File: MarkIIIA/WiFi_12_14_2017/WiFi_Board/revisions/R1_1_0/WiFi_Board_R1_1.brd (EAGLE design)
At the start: 50.8 x 43.2 mm, 29 parts, among them P1 POWER_JACKPTH, P2 USB-B1HSB6, P3 44764-1201

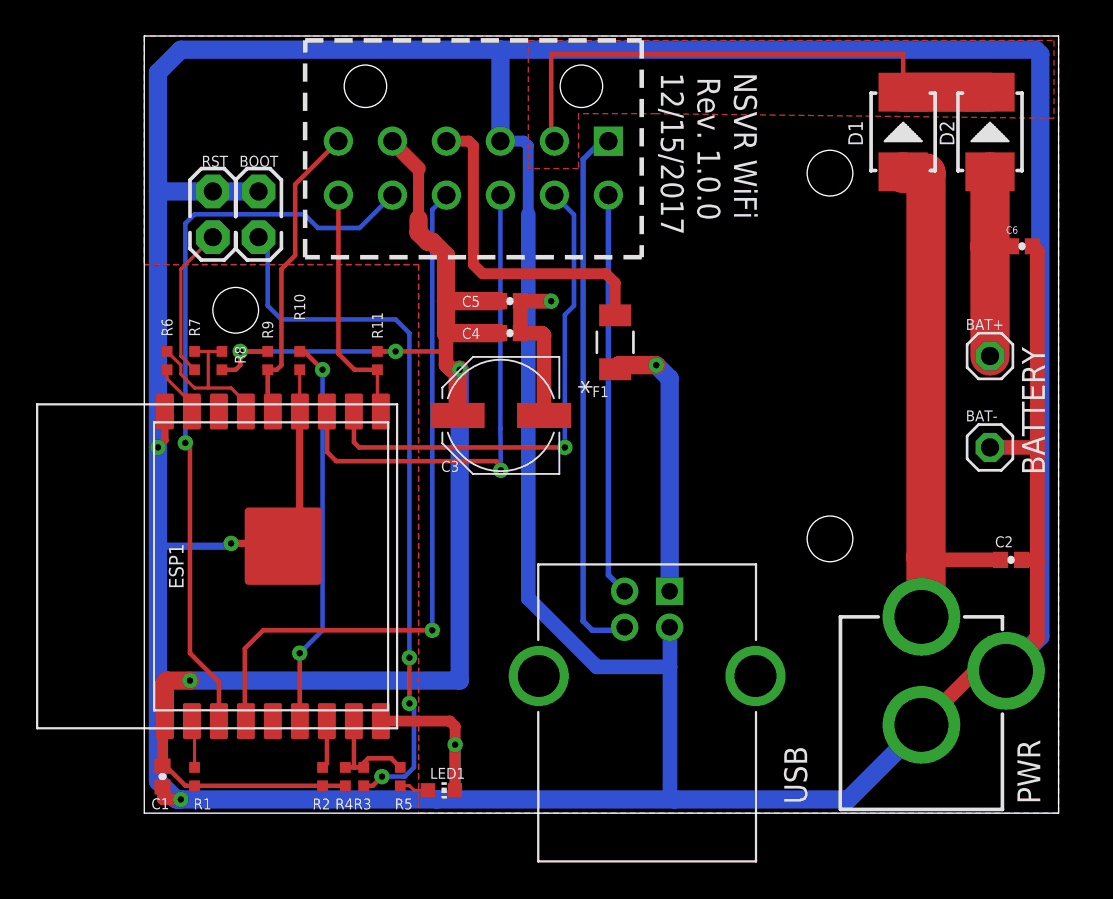
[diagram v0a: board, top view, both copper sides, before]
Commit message: Revise WiFi Board to increase Case Clearance
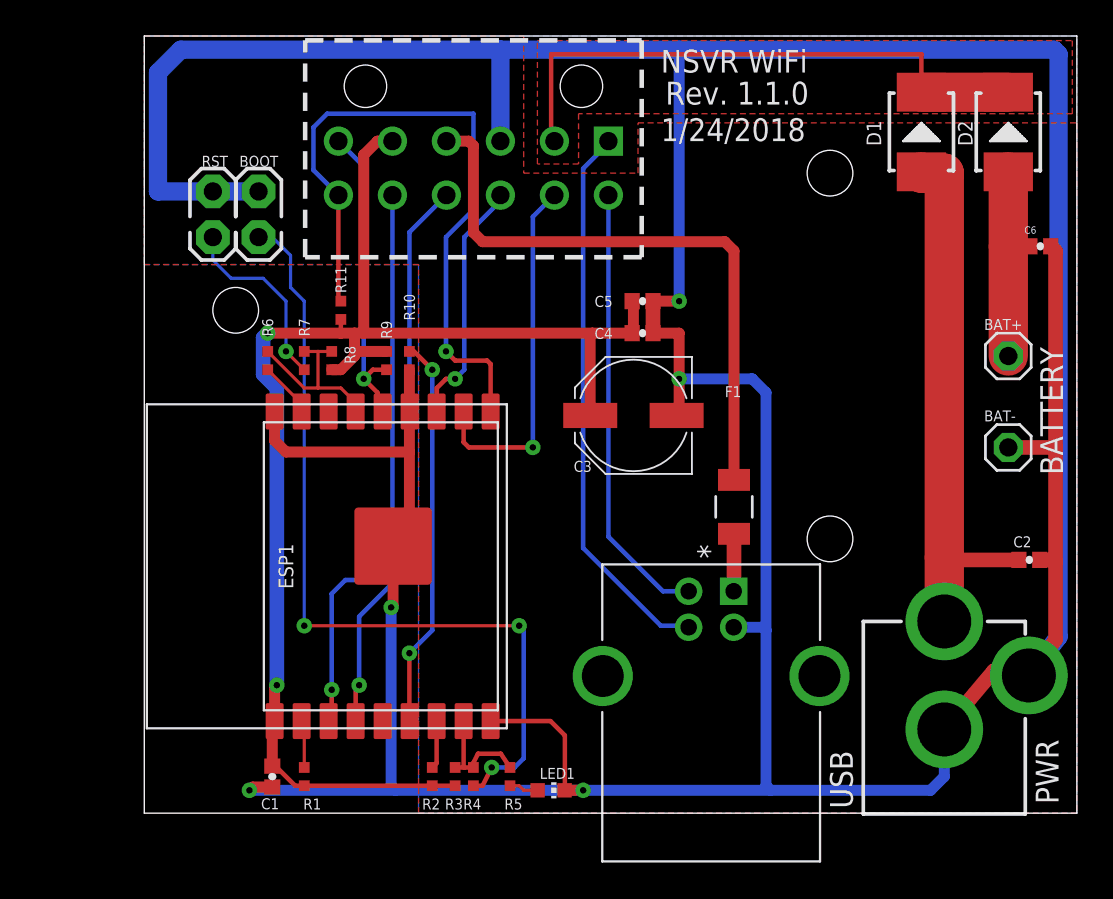
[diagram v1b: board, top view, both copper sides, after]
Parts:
- R3: value 220 -> 10k
- R4: value 10k -> 220
- moved F1 11.3 mm to (32.8, 17.0)
- moved C3 7.37 mm to (27.2, 22.1)
- moved C4 7.37 mm to (27.7, 26.7)
- moved C5 7.37 mm to (27.7, 28.4)
- moved R4 7.11 mm to (18.3, 2.03)
- moved R9 6.60 mm to (13.5, 25.1)
- moved C1 6.10 mm to (7.11, 2.03)
- moved ESP1 6.10 mm to (9.14, 13.7)
- moved LED1 6.10 mm to (22.6, 1.27)
- moved R1 6.10 mm to (8.89, 2.03)
- moved R10 6.10 mm to (14.7, 25.1)
- moved R5 6.10 mm to (20.3, 2.03)
- moved R7 6.10 mm to (8.89, 25.1)
- moved R8 6.10 mm to (10.4, 25.1)
- moved R2 6.10 mm to (16.0, 2.03)
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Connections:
- net 3V3_EXT: now also R3.2; no longer R4.2
- net N$2: now also R4.2; no longer R3.2
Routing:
- net GND: track 303.3 -> 274.8 mm
- net I2C_SDA: track 13.8 -> 38.7 mm, vias 0 -> 1
- net 5V0: track 18.3 -> 34.1 mm
- net TXD0: track 27.8 -> 13.8 mm
- net VBUS_IN: track 15.3 -> 3.20 mm, vias 1 -> 0
- net 3V3_EXT: track 89.3 -> 79.2 mm, vias 4 -> 2
- net RTS0: track 41.2 -> 31.6 mm
- net CTS0: track 39.4 -> 31.3 mm
- net RXD0: track 28.2 -> 20.2 mm
- net N$2: track 40.0 -> 46.1 mm
- net USB_DM: track 22.4 -> 24.7 mm
- net N$1: track 8.42 -> 10.5 mm, vias 0 -> 1
- net VIN: track 31.5 -> 32.5 mm
- net USB_DP: track 30.1 -> 30.9 mm
- net I2C_SCL: track 17.1 -> 17.5 mm, vias 0 -> 1
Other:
- board size 50.8 x 43.2 mm -> 51.8 x 43.2 mm
- board text added: "1/24/2018"
- board text added: "Rev. 1.1.0"
- board text removed: "12/15/2017"
- board text removed: "Rev. 1.0.0"
